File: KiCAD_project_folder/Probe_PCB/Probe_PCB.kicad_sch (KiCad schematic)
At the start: 0 parts

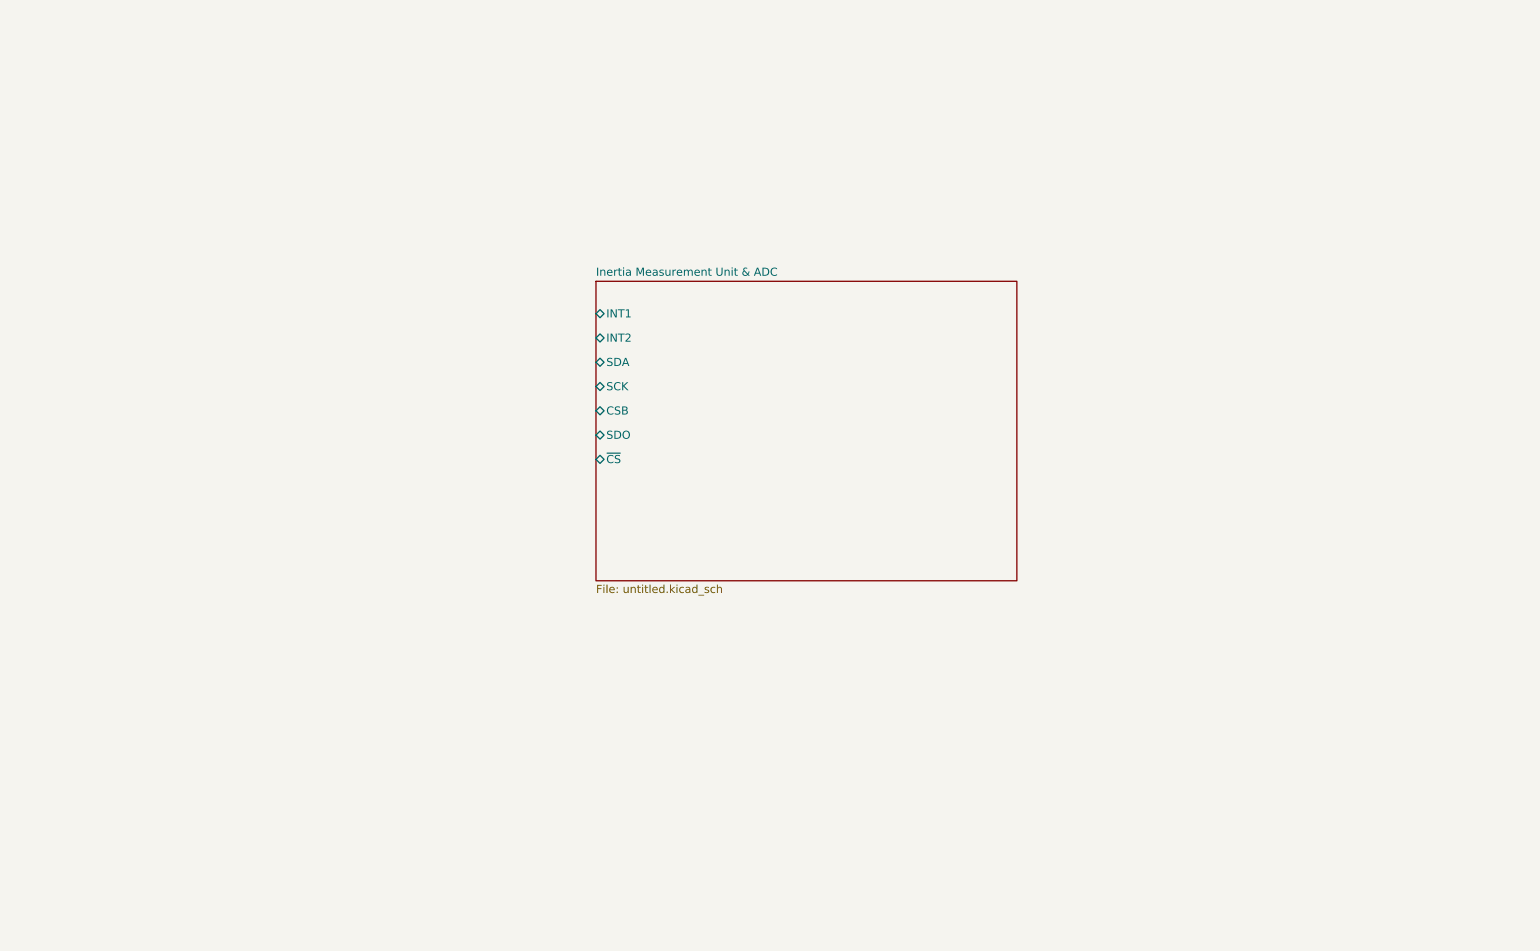
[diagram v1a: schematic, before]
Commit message: added new squeletton for probe pcb
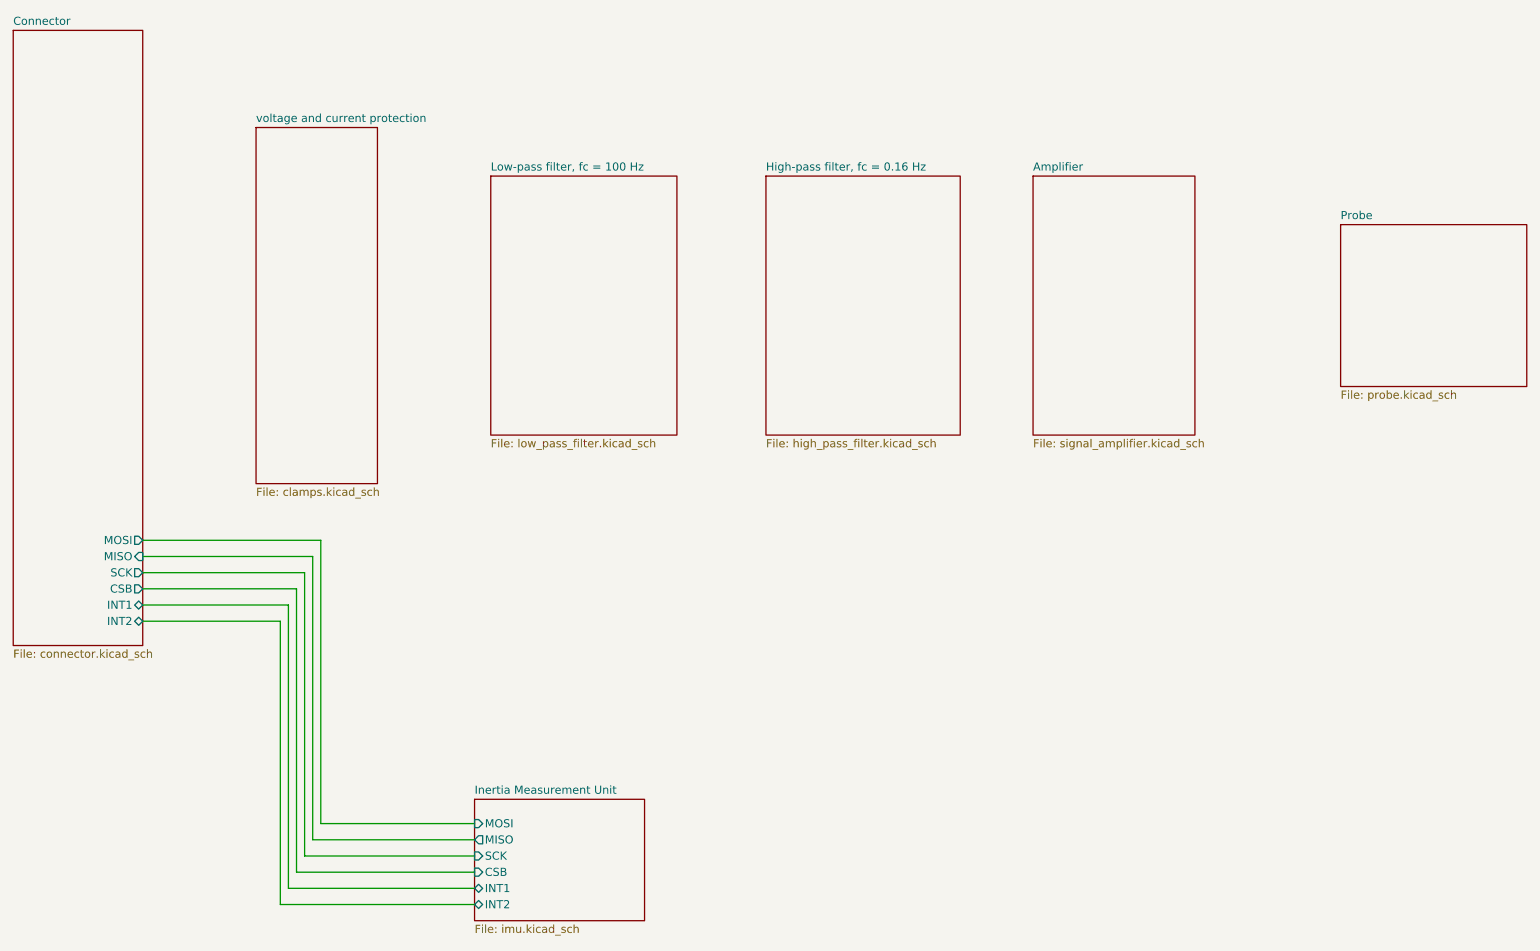
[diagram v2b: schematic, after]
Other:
- sheet Inertia Measurement Unit & ADC renamed Inertia Measurement Unit
- added sheet Amplifier (signal_amplifier.kicad_sch)
- added sheet Connector (connector.kicad_sch)
- added sheet High-pass filter, fc = 0.16 Hz (high_pass_filter.kicad_sch)
- added sheet Low-pass filter, fc = 100 Hz (low_pass_filter.kicad_sch)
- added sheet Probe (probe.kicad_sch)
- added sheet voltage and current protection (clamps.kicad_sch)
- sheet Inertia Measurement Unit: file untitled.kicad_sch -> imu.kicad_sch
- sheet Inertia Measurement Unit ports: added MISO, MOSI; removed SDA, SDO, ~{CS}

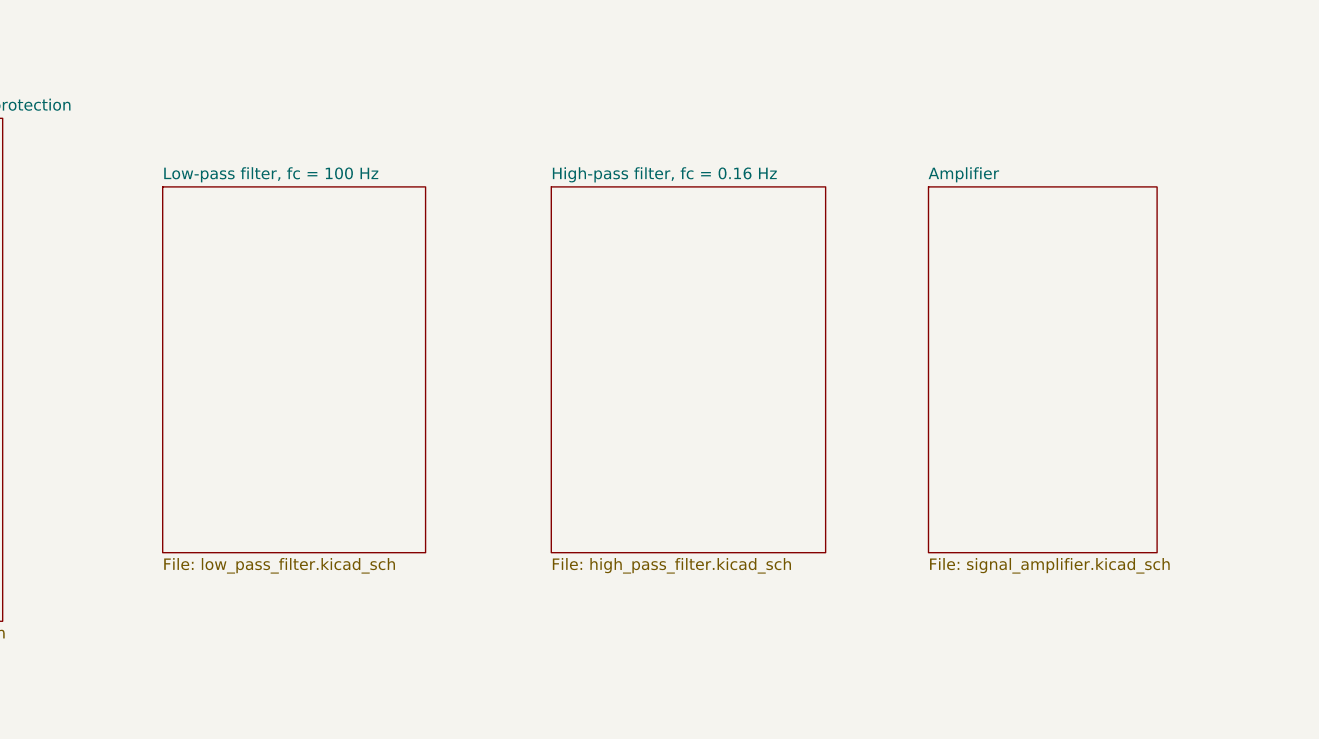
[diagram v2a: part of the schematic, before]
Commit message: added schematic for filters and amplifier
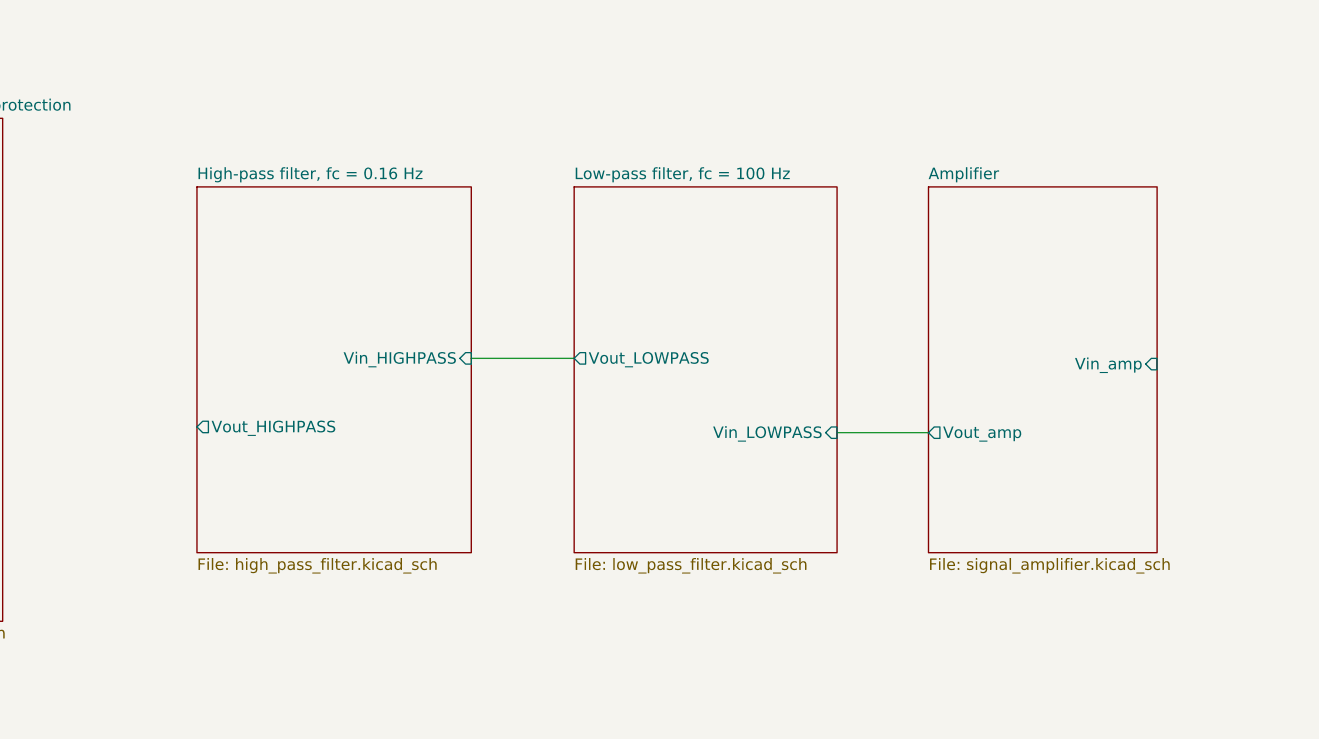
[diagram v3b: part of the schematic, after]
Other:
- sheet Amplifier ports: added Vin_amp, Vout_amp; removed none
- sheet High-pass filter, fc = 0.16 Hz ports: added Vin_HIGHPASS, Vout_HIGHPASS; removed none
- sheet Low-pass filter, fc = 100 Hz ports: added Vin_LOWPASS, Vout_LOWPASS; removed none
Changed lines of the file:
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@@
+    (stroke (width 0) (type default))
+  )
+  (wire (pts (xy 172.72 73.025) (xy 182.88 73.025))
     (stroke (width 0) (type default))
   )
@@
     (stroke (width 0) (type default))
   )
+  (wire (pts (xy 132.08 64.77) (xy 143.51 64.77))
+    (stroke (width 0) (type default))
+  )
   (wire (pts (xy 64.77 115.57) (xy 43.18 115.57))
     (stroke (width 0) (type default))
@@
     (stroke (width 0) (type default))
   )
-  (sheet (at 97.79 45.72) (size 29.21 40.64) (fields_autoplaced)
-    (stroke (width 0.1524) (type solid))
-    (fill (color 0 0 0 0.0000))
-    (property "Sheetname" "Low-pass filter, fc = 100 Hz" (at 97.79 45.0084 0)
-      (effects (font (size 1.27 1.27)) (justify left bottom))
-    )
-    (property "Sheetfile" "low_pass_filter.kicad_sch" (at 97.79 86.9446 0)
-      (effects (font (size 1.27 1.27)) (justify left top))
-    )
-    (property "Champ2" "" (at 97.79 45.72 0)
-      (effects (font (size 1.27 1.27)) hide)
+  (sheet (at 143.51 45.72) (size 29.21 40.64) (fields_autoplaced)
+    (stroke (width 0.1524) (type solid))
+    (fill (color 0 0 0 0.0000))
+    (property "Sheetname" "Low-pass filter, fc = 100 Hz" (at 143.51 45.0084 0)
+      (effects (font (size 1.27 1.27)) (justify left bottom))
+    )
+    (property "Sheetfile" "low_pass_filter.kicad_sch" (at 143.51 86.9446 0)
+      (effects (font (size 1.27 1.27)) (justify left top))
+    )
+    (property "Champ2" "" (at 143.51 45.72 0)
+      (effects (font (size 1.27 1.27)) hide)
+    )
+    (pin "Vout_LOWPASS" output (at 143.51 64.77 180)
+      (effects (font (size 1.27 1.27)) (justify left))
+    )
+    (pin "Vin_LOWPASS" input (at 172.72 73.025 0)
+      (effects (font (size 1.27 1.27)) (justify right))
     )
     (instances
@@
     )
   )
-  (sheet (at 140.97 45.72) (size 30.48 40.64) (fields_autoplaced)
-    (stroke (width 0.1524) (type solid))
-    (fill (color 0 0 0 0.0000))
-    (property "Sheetname" "High-pass filter, fc = 0.16 Hz" (at 140.97 45.0084 0)
-      (effects (font (size 1.27 1.27)) (justify left bottom))
-    )
-    (property "Sheetfile" "high_pass_filter.kicad_sch" (at 140.97 86.9446 0)
-      (effects (font (size 1.27 1.27)) (justify left top))
-    )
-    (property "Champ2" "" (at 140.97 45.72 0)
-      (effects (font (size 1.27 1.27)) hide)
+  (sheet (at 101.6 45.72) (size 30.48 40.64) (fields_autoplaced)
+    (stroke (width 0.1524) (type solid))
+    (fill (color 0 0 0 0.0000))
+    (property "Sheetname" "High-pass filter, fc = 0.16 Hz" (at 101.6 45.0084 0)
+      (effects (font (size 1.27 1.27)) (justify left bottom))
+    )
+    (property "Sheetfile" "high_pass_filter.kicad_sch" (at 101.6 86.9446 0)
+      (effects (font (size 1.27 1.27)) (justify left top))
+    )
+    (property "Champ2" "" (at 101.6 45.72 0)
+      (effects (font (size 1.27 1.27)) hide)
+    )
+    (pin "Vout_HIGHPASS" output (at 101.6 72.39 180)
+      (effects (font (size 1.27 1.27)) (justify left))
+    )
+    (pin "Vin_HIGHPASS" input (at 132.08 64.77 0)
+      (effects (font (size 1.27 1.27)) (justify right))
     )
     (instances
@@
       (effects (font (size 1.27 1.27)) (justify left top))
     )
-    (instances
+    (pin "Vout_amp" output (at 182.88 73.025 180)
+      (effects (font (size 1.27 1.27)) (justify left))
+    )
+    (pin "Vin_amp" input (at 208.28 65.405 0)
+      (effects (font (size 1.27 1.27)) (justify right))
+    )
+    (instances
